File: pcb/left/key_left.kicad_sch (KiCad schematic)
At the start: 141 parts, among them J1 Conn_01x03_Socket, J3 USB_C_Receptacle_USB2.0_16P, Q1 AO3401A, Q2 2N7002, Q3 2N7002, Q4 2N7002, SW1 SW_Push, SW10 SW_Push, SW11 SW_Push, SW12 SW_Push, SW13 SW_Push, SW14 SW_Push, SW15 SW_Push, SW16 SW_Push, SW17 SW_Push, SW18 SW_Push, SW19 SW_Push, SW2 SW_Push, SW20 SW_Push, SW21 SW_Push, SW22 SW_Push, SW23 SW_Push, SW24 SW_Push, SW25 SW_Push, SW26 SW_BOOT, SW3 SW_Push, SW4 SW_Push, SW5 SW_Push, SW6 SW_Push, SW7 SW_Push, SW8 SW_Push, SW9 SW_Push, U1 CH552E, U2 MDBT50Q-1MV2, U3 IS31FL3733-TQ, U4 BQ24074RGT, U5 FSUSB42UMX-TP, U6 SN74LVC1T45DBV, U7 TUSB320, U8 TXS0101DBV, U9 SRV05-4

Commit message: Improved IS31FL3733 decouplers AVCC/DVCC pins
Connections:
- net AVCC_DVCC renamed VCC_SYS
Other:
- moved on the sheet: C10, R22

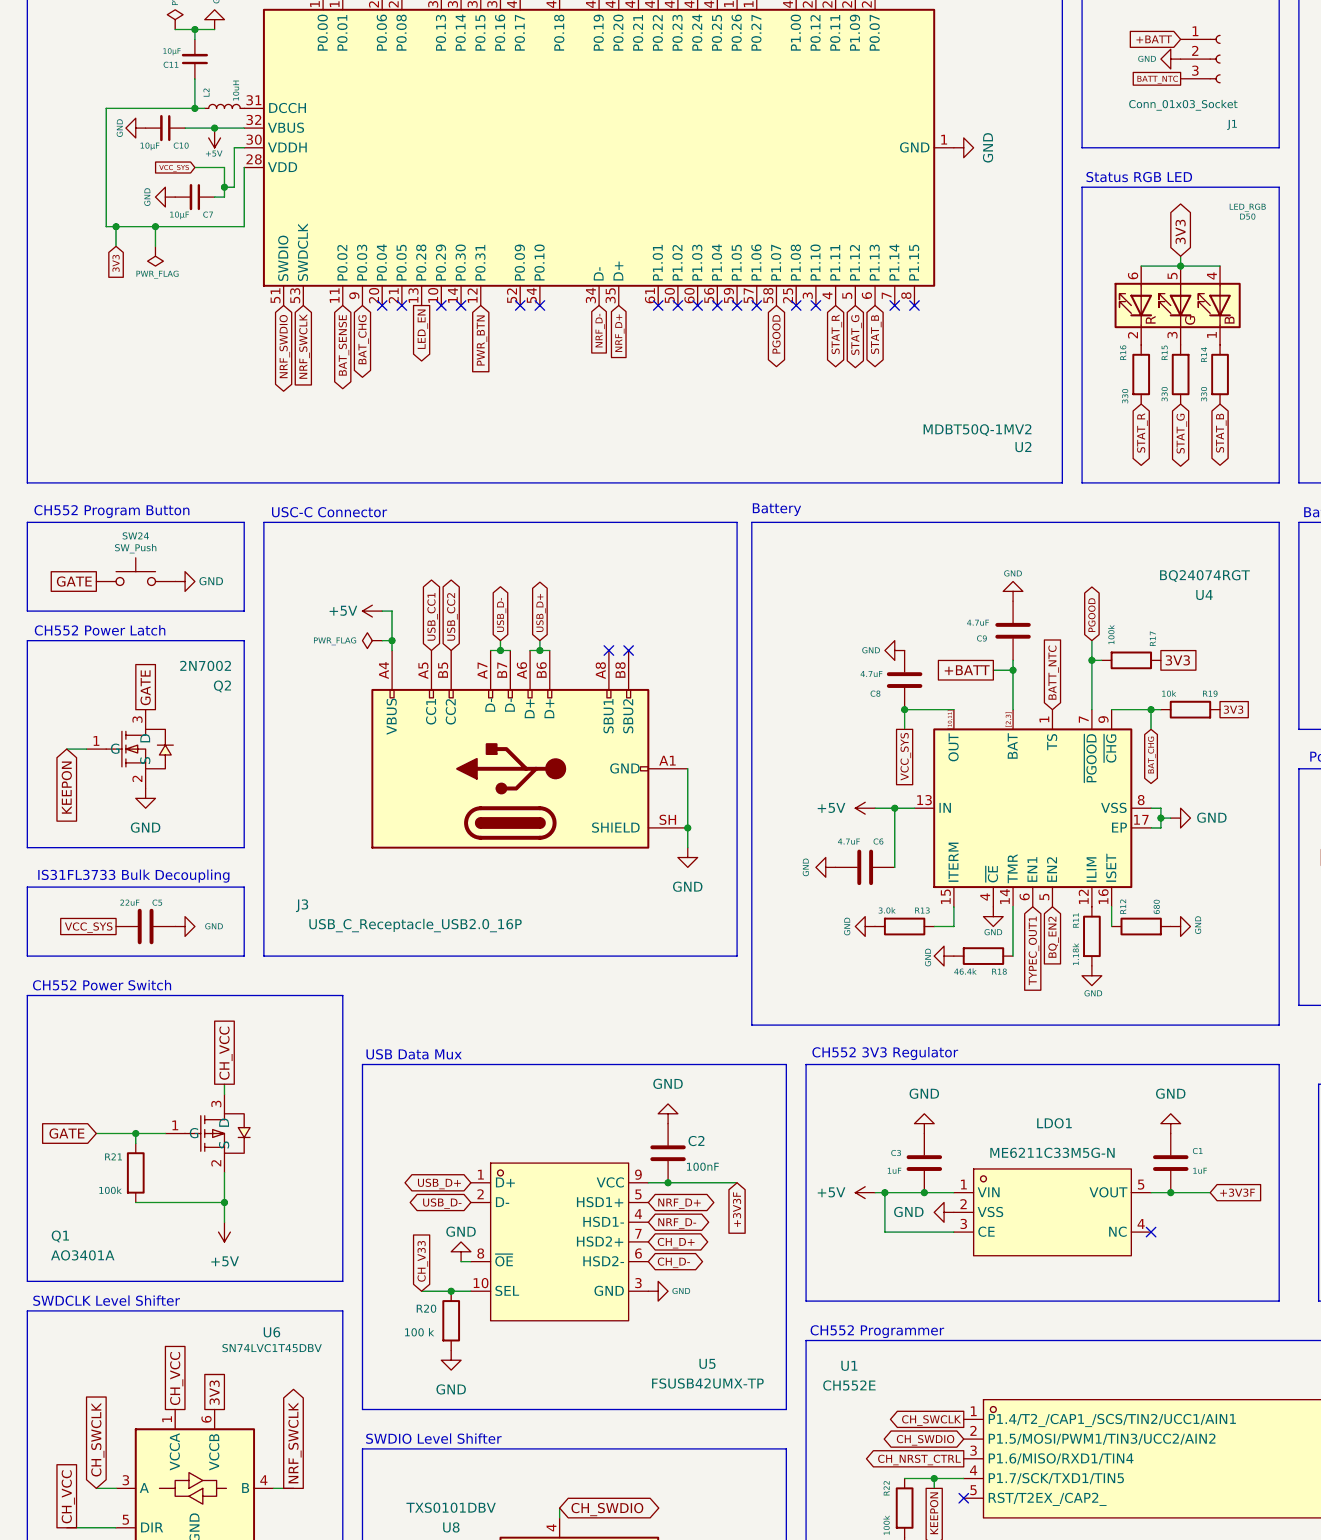
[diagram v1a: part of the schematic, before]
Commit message: Resistor added to BAT_CHG. Schematic ready for PCB placement
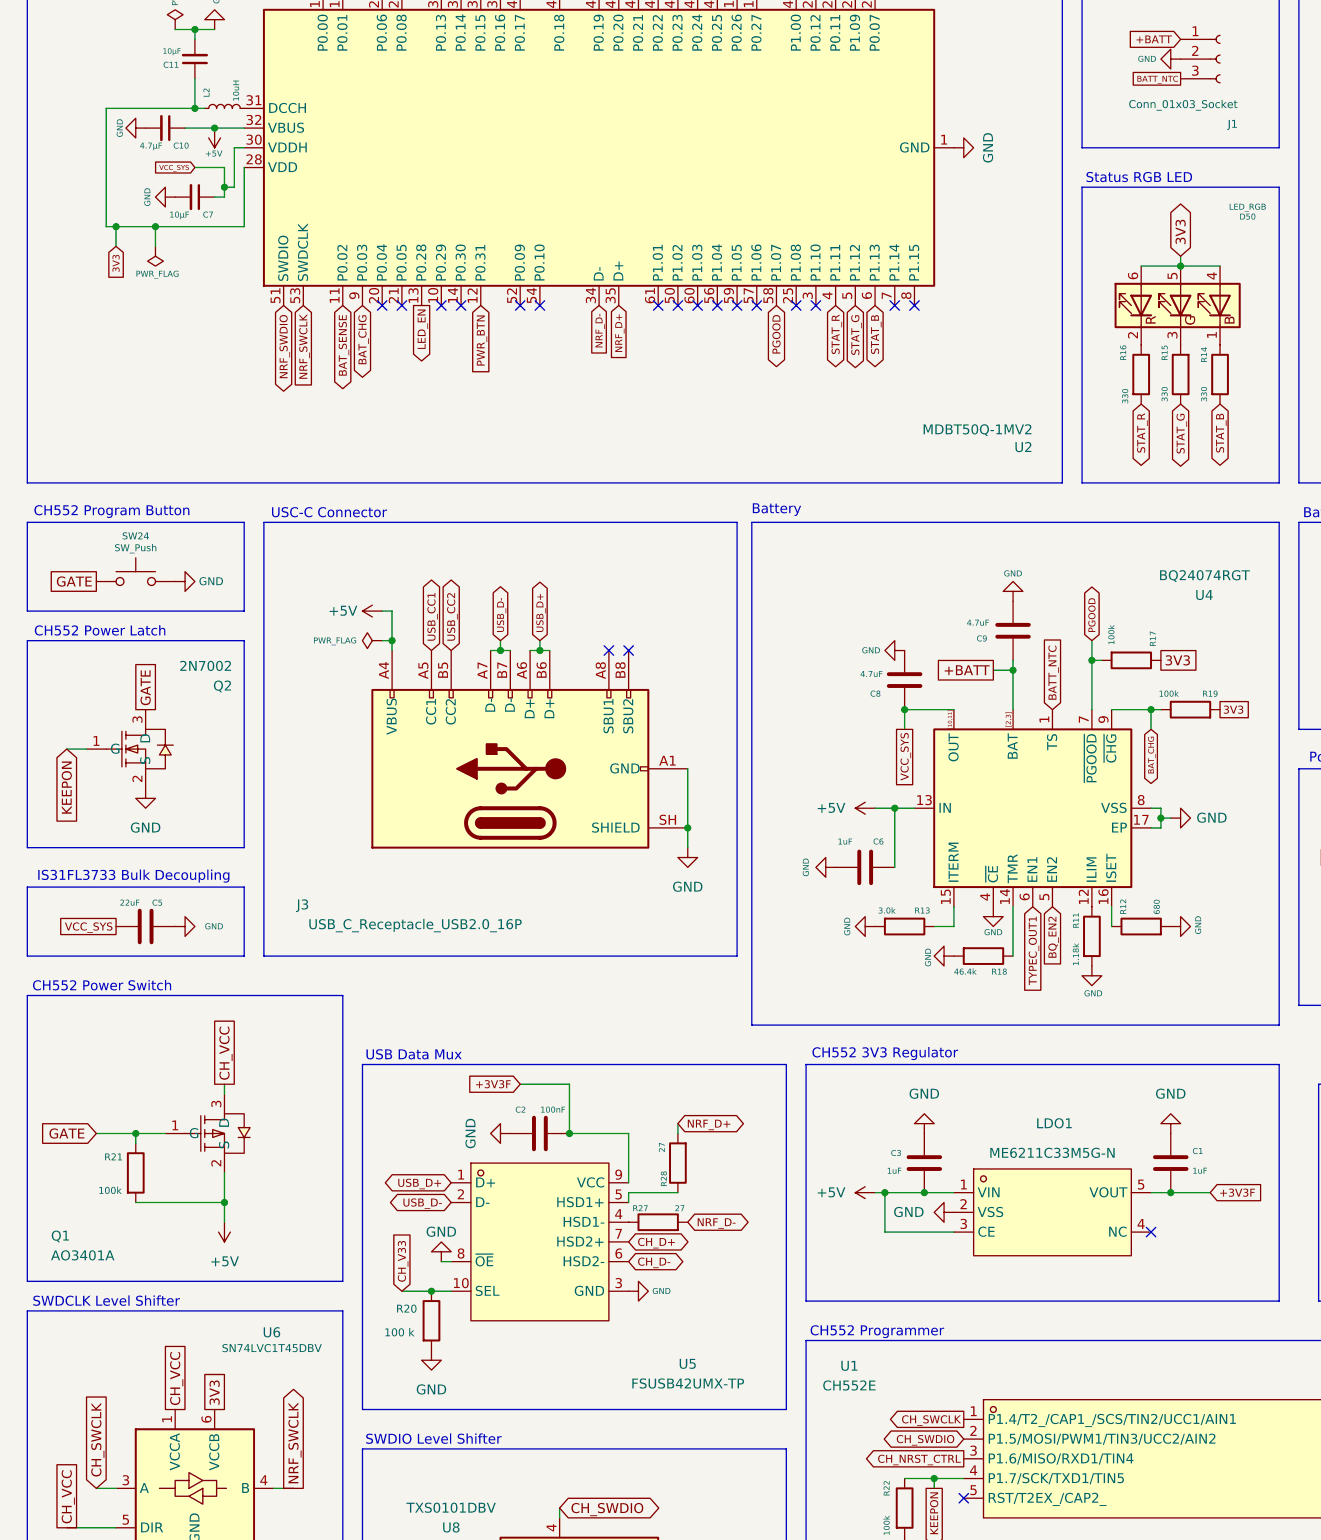
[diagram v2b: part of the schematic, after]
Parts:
- added R27, R28: 27, Resistor_SMD:R_0603_1608Metric, symbol Device:R
- C10: value 10µF -> 4.7µF
- C6: value 4.7uF -> 1uF
- R19: value 10k -> 100k
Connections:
- net NRF_D+: now also R28.2; no longer U5.5 (HSD1+)
- net NRF_D-: now also R27.2; no longer U5.4 (HSD1-)
- new net: R27.1, U5.4 (HSD1-)
- new net: R28.1, U5.5 (HSD1+)
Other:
- moved on the sheet: C2, R20, U5

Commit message: LED replacement to Kingbright APTF1616LSEKJ3ZGKQBC
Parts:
- D1: footprint axseem:D_SOD-123_HandSoldering_Reversible -> RexKeys:D_SOD-123_HandSoldering_Reversible
- D24: footprint LED_SMD:LED_RGB_5050-6 -> RexKeys:LED-SMD_4P-L1.6-W1.6_APTF1616SEJ3ZGGVBDC; symbol LED_RGB_5050:LED_RGB_5050 -> Device:LED_KRGB
- J1: footprint (none) -> Connector_JST:JST_PH_B3B-PH-K_1x03_P2.00mm_Vertical
- SW1: footprint axseem:SW_MX_Choc_Hotswap_Plated -> RexKeys:MX+KailhChoc+GateronKS_Tight
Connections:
- net CS3: now also D24.4 (BA); no longer D24.1 (BK)
- net LED_R1: now also D24.1 (K); no longer D24.4 (BA), D24.5 (GA), D24.6 (RA)
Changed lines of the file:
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@@
 		)
 	)
-	(global_label "LED_R1"
-		(shape bidirectional)
-		(at 252.73 130.81 0)
-		(effects
-			(font
-				(size 1.27 1.27)
-			)
-			(justify left)
-		)
-		(property "Intersheetrefs" "${INTERSHEET_REFS}"
-			(at 252.73 130.81 0)
-			(hide yes)
-			(show_name no)
-			(do_not_autoplace no)
-			(effects
-				(font
-					(size 1.27 1.27)
-				)
-			)
-		)
-	)
 	(global_label "CS13"
 		(shape bidirectional)
@@
 		)
 	)
-	(global_label "LED_R1"
-		(shape bidirectional)
-		(at 252.73 120.65 0)
-		(effects
-			(font
-				(size 1.27 1.27)
-			)
-			(justify left)
-		)
-		(property "Intersheetrefs" "${INTERSHEET_REFS}"
-			(at 252.73 120.65 0)
-			(hide yes)
-			(show_name no)
-			(do_not_autoplace no)
-			(effects
-				(font
-					(size 1.27 1.27)
-				)
-			)
-		)
-	)
 	(global_label "TYPEC_OUT1"
 		(shape input)
@@
 			)
 		)
-		(property "Footprint" "axseem:SW_MX_Choc_Hotswap_Plated"
+		(property "Footprint" "RexKeys:MX+KailhChoc+GateronKS_Tight"
 			(at 200.66 48.26 0)
 			(hide yes)
@@
 	)
 	(symbol
-		(lib_id "LED_RGB_5050:LED_RGB_5050")
+		(lib_id "Device:LED_KRGB")
 		(at 247.65 125.73 0)
+		(mirror y)
 		(unit 1)
 		(body_style 1)
@@
 			)
 		)
-		(property "Footprint" "LED_SMD:LED_RGB_5050-6"
+		(property "Footprint" "RexKeys:LED-SMD_4P-L1.6-W1.6_APTF1616SEJ3ZGGVBDC"
 			(at 247.65 127 0)
 			(hide yes)
@@
 			)
 		)
-		(property "Description" "RGB LED, 6 pin package"
+		(property "Description" "RGB LED, cathode/red/green/blue"
 			(at 247.65 125.73 0)
 			(hide yes)
@@
 		(pin "4"
 		)
-		(pin "5"
-		)
-		(pin "6"
-		)
 		(instances
 			(project "key_left"
@@
 			)
 		)
-		(property "Footprint" ""
+		(property "Footprint" "Connector_JST:JST_PH_B3B-PH-K_1x03_P2.00mm_Vertical"
 			(at 170.18 50.8 0)
 			(hide yes)
@@
 			)
 		)
-		(property "Footprint" "axseem:D_SOD-123_HandSoldering_Reversible"
+		(property "Footprint" "RexKeys:D_SOD-123_HandSoldering_Reversible"
 			(at 205.74 57.15 0)
 			(hide yes)
